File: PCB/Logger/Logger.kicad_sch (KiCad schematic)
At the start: 73 parts, among them J2 USB-C-Socket-V, J3 JST-PH-SM4-TB, J3 USB-PROG, J5 Conn_01x05, J6 TF_PUSH, J8 Shelly, Q1 C179347, Q4 CJ2301, U1 TP4054, U10 ESP32-S3-MINI-1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

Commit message: ESD
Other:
- moved on the sheet: D27
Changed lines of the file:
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@@
     (stroke (width 0) (type default))
   )
+  (wire (pts (xy 81.915 118.745) (xy 81.915 123.19))
+    (stroke (width 0) (type default))
+  )
   (wire (pts (xy 167.64 161.925) (xy 173.355 161.925))
     (stroke (width 0) (type default))
@@
     (stroke (width 0) (type default))
   )
+  (wire (pts (xy 81.915 130.175) (xy 81.915 125.73))
+    (stroke (width 0) (type default))
+  )
+  (wire (pts (xy 71.12 118.11) (xy 71.12 120.65))
+    (stroke (width 0) (type default))
+  )
   (wire (pts (xy 48.895 154.305) (xy 54.61 154.305))
     (stroke (width 0) (type default))
@@
     (stroke (width 0) (type default))
   )
+  (wire (pts (xy 71.12 130.175) (xy 71.12 128.27))
+    (stroke (width 0) (type default))
+  )
   (wire (pts (xy 81.28 154.305) (xy 86.995 154.305))
     (stroke (width 0) (type default))
@@
     )
   )
-  (symbol (lib_id "RevK:ES05D1MC10") (at 81.915 119.38 90) (unit 1)
+  (symbol (lib_id "RevK:ES05D1MC10") (at 81.915 114.935 90) (unit 1)
     (in_bom yes) (on_board yes) (dnp no)
-    (property "Reference" "D27" (at 75.565 119.38 90)
+    (property "Reference" "D27" (at 75.565 114.935 90)
       (effects (font (size 1.27 1.27)) (justify right))
     )
-    (property "Value" "~" (at 81.915 119.38 0)
+    (property "Value" "~" (at 81.915 114.935 0)
       (effects (font (size 1.27 1.27)))
     )
-    (property "Footprint" "RevK:DFN1006-2L" (at 78.74 118.745 0)
+    (property "Footprint" "RevK:DFN1006-2L" (at 78.74 114.3 0)
       (effects (font (size 1.27 1.27)) hide)
     )
-    (property "Datasheet" "" (at 81.915 119.38 0)
+    (property "Datasheet" "" (at 81.915 114.935 0)
       (effects (font (size 1.27 1.27)) hide)
     )
-    (property "LCSC Part #" "C5137770" (at 85.09 119.38 0)
+    (property "LCSC Part #" "C5137770" (at 85.09 114.935 0)
       (effects (font (size 1.27 1.27)) hide)
     )
@@
     )
   )
-  (symbol (lib_id "RevK:ES05D1MC10") (at 71.12 132.08 270) (unit 1)
+  (symbol (lib_id "RevK:ES05D1MC10") (at 71.12 133.985 270) (unit 1)
     (in_bom yes) (on_board yes) (dnp no)
-    (property "Reference" "D27" (at 77.47 132.08 90)
+    (property "Reference" "D27" (at 77.47 133.985 90)
       (effects (font (size 1.27 1.27)) (justify right))
     )
-    (property "Value" "~" (at 71.12 132.08 0)
+    (property "Value" "~" (at 71.12 133.985 0)
       (effects (font (size 1.27 1.27)))
     )
-    (property "Footprint" "RevK:DFN1006-2L" (at 74.295 132.715 0)
+    (property "Footprint" "RevK:DFN1006-2L" (at 74.295 134.62 0)
       (effects (font (size 1.27 1.27)) hide)
     )
-    (property "Datasheet" "" (at 71.12 132.08 0)
+    (property "Datasheet" "" (at 71.12 133.985 0)
       (effects (font (size 1.27 1.27)) hide)
     )
-    (property "LCSC Part #" "C5137770" (at 67.945 132.08 0)
+    (property "LCSC Part #" "C5137770" (at 67.945 133.985 0)
       (effects (font (size 1.27 1.27)) hide)
     )
@@
     )
   )
-  (symbol (lib_id "power:GND") (at 71.12 135.89 0) (unit 1)
+  (symbol (lib_id "power:GND") (at 71.12 137.795 0) (unit 1)
     (in_bom yes) (on_board yes) (dnp no) (fields_autoplaced)
-    (property "Reference" "#PWR0102" (at 71.12 142.24 0)
+    (property "Reference" "#PWR0102" (at 71.12 144.145 0)
       (effects (font (size 1.27 1.27)) hide)
     )
-    (property "Value" "GND" (at 71.12 140.0231 0)
+    (property "Value" "GND" (at 71.12 141.9281 0)
       (effects (font (size 1.27 1.27)))
     )
-    (property "Footprint" "" (at 71.12 135.89 0)
+    (property "Footprint" "" (at 71.12 137.795 0)
       (effects (font (size 1.27 1.27)) hide)
     )
-    (property "Datasheet" "" (at 71.12 135.89 0)
+    (property "Datasheet" "" (at 71.12 137.795 0)
       (effects (font (size 1.27 1.27)) hide)
     )
@@
     )
   )
-  (symbol (lib_id "power:GND") (at 81.915 115.57 180) (unit 1)
+  (symbol (lib_id "power:GND") (at 81.915 111.125 180) (unit 1)
     (in_bom yes) (on_board yes) (dnp no) (fields_autoplaced)
-    (property "Reference" "#PWR0102" (at 81.915 109.22 0)
+    (property "Reference" "#PWR0102" (at 81.915 104.775 0)
       (effects (font (size 1.27 1.27)) hide)
     )
-    (property "Value" "GND" (at 81.915 111.4369 0)
+    (property "Value" "GND" (at 81.915 106.9919 0)
       (effects (font (size 1.27 1.27)))
     )
-    (property "Footprint" "" (at 81.915 115.57 0)
+    (property "Footprint" "" (at 81.915 111.125 0)
       (effects (font (size 1.27 1.27)) hide)
     )
-    (property "Datasheet" "" (at 81.915 115.57 0)
+    (property "Datasheet" "" (at 81.915 111.125 0)
       (effects (font (size 1.27 1.27)) hide)
     )
@@
     )
   )
-  (symbol (lib_id "RevK:ES05D1MC10") (at 81.915 129.54 270) (unit 1)
+  (symbol (lib_id "RevK:ES05D1MC10") (at 81.915 133.985 270) (unit 1)
     (in_bom yes) (on_board yes) (dnp no)
-    (property "Reference" "D27" (at 88.265 129.54 90)
+    (property "Reference" "D27" (at 88.265 133.985 90)
       (effects (font (size 1.27 1.27)) (justify right))
     )
-    (property "Value" "~" (at 81.915 129.54 0)
+    (property "Value" "~" (at 81.915 133.985 0)
       (effects (font (size 1.27 1.27)))
     )
-    (property "Footprint" "RevK:DFN1006-2L" (at 85.09 130.175 0)
+    (property "Footprint" "RevK:DFN1006-2L" (at 85.09 134.62 0)
       (effects (font (size 1.27 1.27)) hide)
     )
-    (property "Datasheet" "" (at 81.915 129.54 0)
+    (property "Datasheet" "" (at 81.915 133.985 0)
       (effects (font (size 1.27 1.27)) hide)
     )
-    (property "LCSC Part #" "C5137770" (at 78.74 129.54 0)
+    (property "LCSC Part #" "C5137770" (at 78.74 133.985 0)
       (effects (font (size 1.27 1.27)) hide)
     )
@@
     )
   )
-  (symbol (lib_id "RevK:ES05D1MC10") (at 71.12 116.84 90) (unit 1)
+  (symbol (lib_id "RevK:ES05D1MC10") (at 71.12 114.3 90) (unit 1)
     (in_bom yes) (on_board yes) (dnp no)
-    (property "Reference" "D27" (at 64.77 116.84 90)
+    (property "Reference" "D27" (at 64.77 114.3 90)
       (effects (font (size 1.27 1.27)) (justify right))
     )
-    (property "Value" "~" (at 71.12 116.84 0)
+    (property "Value" "~" (at 71.12 114.3 0)
       (effects (font (size 1.27 1.27)))
     )
-    (property "Footprint" "RevK:DFN1006-2L" (at 67.945 116.205 0)
+    (property "Footprint" "RevK:DFN1006-2L" (at 67.945 113.665 0)
       (effects (font (size 1.27 1.27)) hide)
     )
-    (property "Datasheet" "" (at 71.12 116.84 0)
+    (property "Datasheet" "" (at 71.12 114.3 0)
       (effects (font (size 1.27 1.27)) hide)
     )
-    (property "LCSC Part #" "C5137770" (at 74.295 116.84 0)
+    (property "LCSC Part #" "C5137770" (at 74.295 114.3 0)
       (effects (font (size 1.27 1.27)) hide)
     )
@@
     )
   )
-  (symbol (lib_id "power:GND") (at 81.915 133.35 0) (unit 1)
+  (symbol (lib_id "power:GND") (at 81.915 137.795 0) (unit 1)
     (in_bom yes) (on_board yes) (dnp no) (fields_autoplaced)
-    (property "Reference" "#PWR0102" (at 81.915 139.7 0)
+    (property "Reference" "#PWR0102" (at 81.915 144.145 0)
       (effects (font (size 1.27 1.27)) hide)
     )
-    (property "Value" "GND" (at 81.915 137.4831 0)
+    (property "Value" "GND" (at 81.915 141.9281 0)
       (effects (font (size 1.27 1.27)))
     )
-    (property "Footprint" "" (at 81.915 133.35 0)
+    (property "Footprint" "" (at 81.915 137.795 0)
       (effects (font (size 1.27 1.27)) hide)
     )
-    (property "Datasheet" "" (at 81.915 133.35 0)
+    (property "Datasheet" "" (at 81.915 137.795 0)
       (effects (font (size 1.27 1.27)) hide)
     )
@@
     )
   )
-  (symbol (lib_id "power:GND") (at 71.12 113.03 180) (unit 1)
+  (symbol (lib_id "power:GND") (at 71.12 110.49 180) (unit 1)
     (in_bom yes) (on_board yes) (dnp no) (fields_autoplaced)
-    (property "Reference" "#PWR0102" (at 71.12 106.68 0)
+    (property "Reference" "#PWR0102" (at 71.12 104.14 0)
       (effects (font (size 1.27 1.27)) hide)
     )
-    (property "Value" "GND" (at 71.12 108.8969 0)
+    (property "Value" "GND" (at 71.12 106.3569 0)
       (effects (font (size 1.27 1.27)))
     )
-    (property "Footprint" "" (at 71.12 113.03 0)
+    (property "Footprint" "" (at 71.12 110.49 0)
       (effects (font (size 1.27 1.27)) hide)
     )
-    (property "Datasheet" "" (at 71.12 113.03 0)
+    (property "Datasheet" "" (at 71.12 110.49 0)
       (effects (font (size 1.27 1.27)) hide)
     )

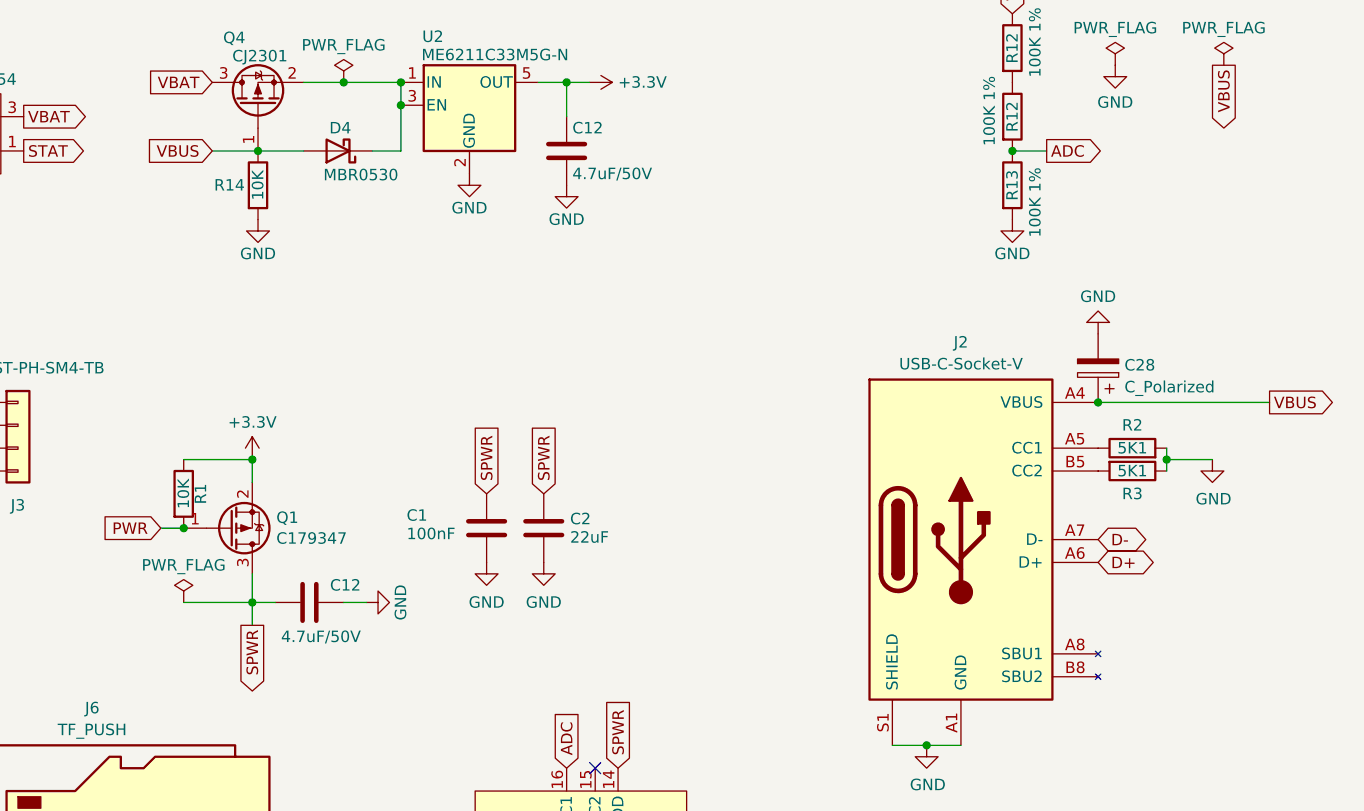
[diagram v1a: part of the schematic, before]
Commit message: More caps
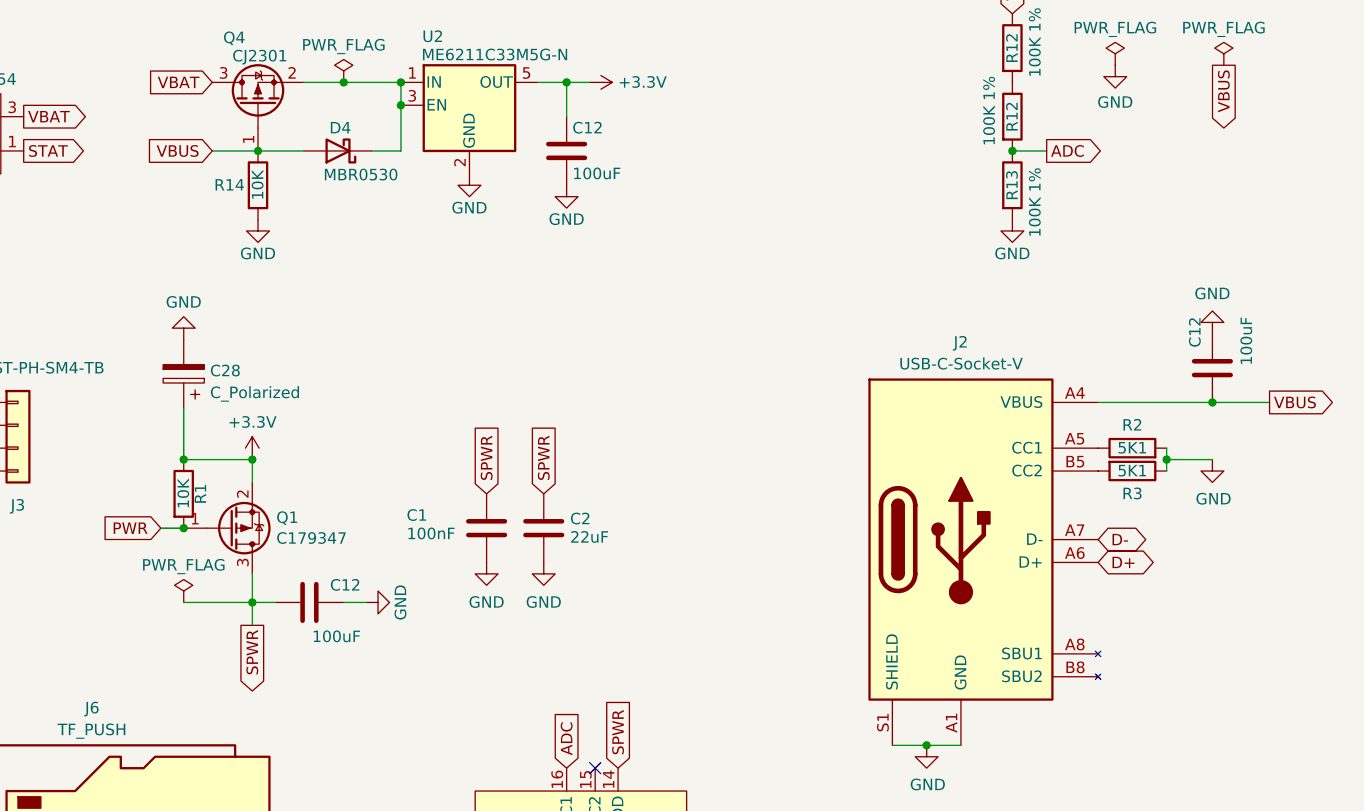
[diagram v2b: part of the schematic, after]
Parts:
- added C12: 100uF, RevK:C_0805, symbol Device:C
- C12: value 4.7uF/50V -> 100uF; LCSC Part # (none) -> C141660
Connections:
- net +3.3V: now also C28.1
- net GND: now also C12.2
- net VBUS: now also C12.1; no longer C28.1
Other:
- moved on the sheet: C28
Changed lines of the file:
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@@
   (junction (at 151.765 161.925) (diameter 0) (color 0 0 0 0)
   )
-  (junction (at 257.175 65.405) (diameter 0) (color 0 0 0 0)
-  )
   (junction (at 167.64 161.925) (diameter 0) (color 0 0 0 0)
   )
@@
   (junction (at 70.485 161.925) (diameter 0) (color 0 0 0 0)
   )
+  (junction (at 155.575 71.755) (diameter 0) (color 0 0 0 0)
+  )
   (junction (at 97.79 154.305) (diameter 0) (color 0 0 0 0)
   )
@@
   (junction (at 146.05 161.925) (diameter 0) (color 0 0 0 0)
   )
+  (junction (at 269.875 65.405) (diameter 0) (color 0 0 0 0)
+  )
   (junction (at 65.405 161.925) (diameter 0) (color 0 0 0 0)
   )
@@
     (stroke (width 0) (type default))
   )
-  (wire (pts (xy 276.225 65.405) (xy 257.175 65.405))
+  (wire (pts (xy 257.175 65.405) (xy 269.875 65.405))
     (stroke (width 0) (type default))
   )
@@
     (stroke (width 0) (type default))
   )
+  (wire (pts (xy 269.875 65.405) (xy 276.225 65.405))
+    (stroke (width 0) (type default))
+  )
   (wire (pts (xy 140.97 154.305) (xy 146.05 154.305))
     (stroke (width 0) (type default))
@@
     (stroke (width 0) (type default))
   )
+  (wire (pts (xy 155.575 66.04) (xy 155.575 71.755))
+    (stroke (width 0) (type default))
+  )
   (wire (pts (xy 151.765 161.925) (xy 156.845 161.925))
     (stroke (width 0) (type default))
@@
       (effects (font (size 1.27 1.27)) (justify left))
     )
-    (property "Value" "4.7uF/50V" (at 198.755 40.005 0)
+    (property "Value" "100uF" (at 198.755 40.005 0)
       (effects (font (size 1.27 1.27)) (justify left))
     )
@@
       (effects (font (size 1.27 1.27)) hide)
     )
+    (property "LCSC Part #" "C141660" (at 198.12 37.465 0)
+      (effects (font (size 1.27 1.27)) hide)
+    )
     (pin "1")
     (pin "2")
@@
     )
   )
+  (symbol (lib_id "power:GND") (at 269.875 57.785 180) (unit 1)
+    (in_bom yes) (on_board yes) (dnp no) (fields_autoplaced)
+    (property "Reference" "#PWR013" (at 269.875 51.435 0)
+      (effects (font (size 1.27 1.27)) hide)
+    )
+    (property "Value" "GND" (at 269.875 53.3416 0)
+      (effects (font (size 1.27 1.27)))
+    )
+    (property "Footprint" "" (at 269.875 57.785 0)
+      (effects (font (size 1.27 1.27)) hide)
+    )
+    (property "Datasheet" "" (at 269.875 57.785 0)
+      (effects (font (size 1.27 1.27)) hide)
+    )
+    (pin "1")
+    (instances
+      (project "USBA"
+        (path "/2d210a96-f81f-42a9-8bf4-1b43c11086f3"
+          (reference "#PWR013") (unit 1)
+        )
+      )
+      (project "EPD75"
+        (path "/46c350bb-7de4-4e81-aafd-4af55e37aab0"
+          (reference "#PWR011") (unit 1)
+        )
+      )
+      (project "Logger"
+        (path "/babeabf2-f3b0-4ed5-8d9e-0215947e6cf3"
+          (reference "#PWR041") (unit 1)
+        )
+      )
+    )
+  )
   (symbol (lib_id "Device:C") (at 195.58 79.375 0) (unit 1)
     (in_bom yes) (on_board yes) (dnp no) (fields_autoplaced)
@@
     )
   )
-  (symbol (lib_id "Device:C_Polarized") (at 257.175 61.595 180) (unit 1)
+  (symbol (lib_id "Device:C_Polarized") (at 155.575 62.23 180) (unit 1)
     (in_bom yes) (on_board yes) (dnp no) (fields_autoplaced)
-    (property "Reference" "C28" (at 260.096 61.2719 0)
+    (property "Reference" "C28" (at 158.496 61.9069 0)
       (effects (font (size 1.27 1.27)) (justify right))
     )
-    (property "Value" "C_Polarized" (at 260.096 63.6961 0)
+    (property "Value" "C_Polarized" (at 158.496 64.3311 0)
       (effects (font (size 1.27 1.27)) (justify right))
     )
-    (property "Footprint" "RevK:CP_EIA-7343-31_Kemet-D" (at 256.2098 57.785 0)
+    (property "Footprint" "RevK:CP_EIA-7343-31_Kemet-D" (at 154.6098 58.42 0)
       (effects (font (size 1.27 1.27)) hide)
     )
-    (property "Datasheet" "~" (at 257.175 61.595 0)
+    (property "Datasheet" "~" (at 155.575 62.23 0)
       (effects (font (size 1.27 1.27)) hide)
     )
-    (property "LCSC Part #" "C106188" (at 257.175 61.595 0)
+    (property "LCSC Part #" "C106188" (at 155.575 62.23 0)
       (effects (font (size 1.27 1.27)) hide)
     )
-    (property "JLCPCB Rotation Offset" "180" (at 257.175 61.595 0)
+    (property "JLCPCB Rotation Offset" "180" (at 155.575 62.23 0)
       (effects (font (size 1.27 1.27)) hide)
     )
@@
       (effects (font (size 1.27 1.27)) (justify left))
     )
-    (property "Value" "4.7uF/50V" (at 175.26 91.44 90)
+    (property "Value" "100uF" (at 175.26 91.44 90)
       (effects (font (size 1.27 1.27)) (justify left))
     )
@@
       (effects (font (size 1.27 1.27)) hide)
     )
+    (property "LCSC Part #" "C141660" (at 169.545 87.63 90)
+      (effects (font (size 1.27 1.27)) hide)
+    )
     (pin "1")
     (pin "2")
@@
     )
   )
-  (symbol (lib_id "power:GND") (at 257.175 57.785 180) (unit 1)
+  (symbol (lib_id "power:GND") (at 155.575 58.42 180) (unit 1)
     (in_bom yes) (on_board yes) (dnp no) (fields_autoplaced)
-    (property "Reference" "#PWR0105" (at 257.175 51.435 0)
+    (property "Reference" "#PWR0105" (at 155.575 52.07 0)
       (effects (font (size 1.27 1.27)) hide)
     )
-    (property "Value" "GND" (at 257.175 53.6519 0)
+    (property "Value" "GND" (at 155.575 54.2869 0)
       (effects (font (size 1.27 1.27)))
     )
-    (property "Footprint" "" (at 257.175 57.785 0)
+    (property "Footprint" "" (at 155.575 58.42 0)
       (effects (font (size 1.27 1.27)) hide)
     )
-    (property "Datasheet" "" (at 257.175 57.785 0)
+    (property "Datasheet" "" (at 155.575 58.42 0)
       (effects (font (size 1.27 1.27)) hide)
     )
@@
         )
       )
+    )
+  )
+  (symbol (lib_id "Device:C") (at 269.875 61.595 180) (unit 1)
+    (in_bom yes) (on_board yes) (dnp no)
+    (property "Reference" "C12" (at 267.97 55.88 90)
+      (effects (font (size 1.27 1.27)) (justify left))
+    )
+    (property "Value" "100uF" (at 273.685 55.88 90)
+      (effects (font (size 1.27 1.27)) (justify left))
+    )
+    (property "Footprint" "RevK:C_0805" (at 268.9098 57.785 0)
+      (effects (font (size 1.27 1.27)) hide)
+    )
+    (property "Datasheet" "~" (at 269.875 61.595 0)
+      (effects (font (size 1.27 1.27)) hide)
+    )
+    (property "LCSC Part #" "C141660" (at 269.875 61.595 90)
+      (effects (font (size 1.27 1.27)) hide)
+    )
+    (pin "1")
+    (pin "2")
+    (instances
+      (project "Watchy"
+        (path "/03039abc-65dd-445c-a352-9e386e1f31aa"
+          (reference "C12") (unit 1)
+        )
+      )
+      (project "EPDBat"
+        (path "/46c350bb-7de4-4e81-aafd-4af55e37aab0"
+          (reference "C19") (unit 1)
+        )
+      )
+      (project "Logger"
+        (path "/babeabf2-f3b0-4ed5-8d9e-0215947e6cf3"
+          (reference "C26") (unit 1)
+        )
+      )

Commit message: Tidy
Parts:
- J5: FC Part (none) -> 1814948; Part Name (none) -> PTSM 0,5/ 5-HH0-2,5-SMD WH R32
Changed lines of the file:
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@@
+      (effects (font (size 1.27 1.27)) hide)
+    )
+    (property "Part Name" "PTSM 0,5/ 5-HH0-2,5-SMD WH R32" (at 48.895 125.73 0)
+      (effects (font (size 1.27 1.27)) hide)
+    )
+    (property "FC Part" "1814948" (at 48.895 125.73 0)
       (effects (font (size 1.27 1.27)) hide)
     )
